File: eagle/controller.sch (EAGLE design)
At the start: 34 parts, among them K1 G5V1, T1 2SC1213, T2 2SC1213, X12 057-040-0

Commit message: First PCB
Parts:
- X1: device con-amp:USB-787616 -> con-ptr500:AK500/2
- X11: device con-ptr500:AK500/2 -> con-ptr500:AK500/3-H
- X12: value 057-040-0 -> (none); device con-panduit:057-040-0 -> con-amp:USB-787616
- X13: value (none) -> 057-040-0; device con-phoenix-254:MPT3 -> con-panduit:057-040-0
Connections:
- net GND: now also X1-2.KL, X12.4, X13-6.S, X2-1.KL; no longer X1.4, X12-6.S, X13-1.1, X2-2.KL
- net N$1: now also X1-1.KL, X2-2.KL; no longer X2-1.KL, X5-2.KL
- net N$13: now also X13-13.S, X8-2.KL; no longer X12-13.S, X3-2.KL
- net N$15: now also X13-15.S, X9-2.KL; no longer X12-15.S, X4-2.KL
- net N$17: now also X13-12.S; no longer X12-12.S
- net N$18: now also X10-2.KL, X13-22.S; no longer X12-22.S, X6-2.KL
- net N$19: now also X13-7.S; no longer X12-7.S
- net N$20: now also X13-1.S; no longer X12-1.S
- net N$21: now also X13-16.S; no longer X12-16.S
- net N$22: now also R1.2, X12.1, X6-2.KL; no longer X1.1, X11-2.KL
- net N$4: now also X11-2.KL, X3-2.KL, X4-2.KL, X5-2.KL; no longer X10-2.KL, X13-2.1, X8-2.KL, X9-2.KL
- net N$5: now also X11-3.KL, X13-39.S; no longer X12-39.S, X13-3.1
- net N$6: now also X13-11.S; no longer X12-11.S
- net N$9: now also X13-18.S; no longer X12-18.S
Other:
- moved on the sheet: X10-1, X10-2, X11-1, X11-2, X2-1, X2-2, X3-1, X3-2, X4-1, X4-2, X5-1, X5-2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

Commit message: Updating PIR
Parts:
- removed R1: 10K, resistor:R-EU_0204/7
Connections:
- net N$22: no longer R1.2
- net N$5: now also X13-37.S; no longer R1.1, X13-39.S
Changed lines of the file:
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@@
 <part name="X13" library="con-panduit" deviceset="057-040-" device="0"/>
 <part name="GND17" library="supply1" deviceset="GND" device=""/>
-<part name="R1" library="resistor" deviceset="R-EU_" device="0204/7" value="10K"/>
 <part name="LED1" library="led" deviceset="LED" device="5MM"/>
 <part name="R2" library="resistor" deviceset="R-EU_" device="0204/7" value="1.5K"/>
@@
 <instance part="X13" gate="-40" x="215.9" y="-40.64"/>
 <instance part="GND17" gate="1" x="142.24" y="-38.1"/>
-<instance part="R1" gate="G$1" x="162.56" y="-10.16" rot="R90"/>
 <instance part="LED1" gate="G$1" x="17.78" y="66.04"/>
 <instance part="R2" gate="G$1" x="17.78" y="50.8" rot="R270"/>
@@
 <wire x1="91.44" y1="71.12" x2="104.14" y2="71.12" width="0.1524" layer="91"/>
 <junction x="104.14" y="71.12"/>
-<wire x1="162.56" y1="-5.08" x2="162.56" y2="71.12" width="0.1524" layer="91"/>
-<wire x1="162.56" y1="71.12" x2="144.78" y2="71.12" width="0.1524" layer="91"/>
-<junction x="144.78" y="71.12"/>
-<pinref part="R1" gate="G$1" pin="2"/>
 </segment>
 </net>
@@
 <net name="N$5" class="0">
 <segment>
-<pinref part="R1" gate="G$1" pin="1"/>
-<wire x1="162.56" y1="-30.48" x2="162.56" y2="-15.24" width="0.1524" layer="91"/>
-<wire x1="162.56" y1="-30.48" x2="187.96" y2="-30.48" width="0.1524" layer="91"/>
-<pinref part="X13" gate="-39" pin="S"/>
-<wire x1="187.96" y1="-30.48" x2="187.96" y2="-40.64" width="0.1524" layer="91"/>
-<wire x1="187.96" y1="-40.64" x2="195.58" y2="-40.64" width="0.1524" layer="91"/>
+<wire x1="157.48" y1="-30.48" x2="190.5" y2="-30.48" width="0.1524" layer="91"/>
 <pinref part="X11" gate="-3" pin="KL"/>
 <wire x1="157.48" y1="-33.02" x2="157.48" y2="-30.48" width="0.1524" layer="91"/>
-<wire x1="157.48" y1="-30.48" x2="162.56" y2="-30.48" width="0.1524" layer="91"/>
-<junction x="162.56" y="-30.48"/>
-</segment>
-</net>
+<wire x1="190.5" y1="-30.48" x2="190.5" y2="-35.56" width="0.1524" layer="91"/>
+<pinref part="X13" gate="-37" pin="S"/>
+<wire x1="190.5" y1="-35.56" x2="195.58" y2="-35.56" width="0.1524" layer="91"/>
+</segment>
+</net>

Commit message: Update
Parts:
- removed T1, T2: 2SC1213, transistor:-NPN-TO92-EBC
- added T3, T4: 2N2222, transistor-neu-to92:2N2222-NPN-TO92-EBC
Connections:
- net GND: now also T3.E, T4.C; no longer T1.E, T2.E
- net N$10: now also T4.B; no longer T1.B
- net N$12: now also T4.E; no longer T1.C
- net N$2: now also T3.B; no longer T2.B
- net N$3: now also T3.C; no longer T2.C
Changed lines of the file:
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@@
 <part name="GND1" library="supply1" deviceset="GND" device=""/>
 <part name="R3" library="resistor" deviceset="R-EU_" device="0204/7" value="1.5K"/>
-<part name="T1" library="transistor" deviceset="*-NPN-" device="TO92-EBC" value="2SC1213"/>
 <part name="R4" library="resistor" deviceset="R-EU_" device="0204/7" value="1.3K"/>
 <part name="R5" library="resistor" deviceset="R-EU_" device="0204/7" value="10K"/>
@@
 <part name="X7" library="con-ptr500" deviceset="AK500/2" device=""/>
 <part name="GND9" library="supply1" deviceset="GND" device=""/>
-<part name="T2" library="transistor" deviceset="*-NPN-" device="TO92-EBC" value="2SC1213"/>
 <part name="R12" library="resistor" deviceset="R-EU_" device="0204/7" value="1.3K"/>
 <part name="GND8" library="supply1" deviceset="GND" device=""/>
@@
 <part name="GND18" library="supply1" deviceset="GND" device=""/>
 <part name="X11" library="con-ptr500" deviceset="AK500/3-H" device=""/>
+<part name="T3" library="transistor-neu-to92" deviceset="*-NPN-" device="TO92-EBC" technology="2N2222" value="2N2222"/>
+<part name="T4" library="transistor-neu-to92" deviceset="*-NPN-" device="TO92-EBC" technology="2N2222" value="2N2222"/>
 </parts>
 <sheets>
@@
 <instance part="GND1" gate="1" x="50.8" y="40.64"/>
 <instance part="R3" gate="G$1" x="7.62" y="15.24" rot="R90"/>
-<instance part="T1" gate="G$1" x="73.66" y="38.1" rot="MR180"/>
 <instance part="R4" gate="G$1" x="91.44" y="25.4" rot="R180"/>
 <instance part="R5" gate="G$1" x="114.3" y="7.62" rot="R90"/>
@@
 <instance part="X7" gate="-2" x="76.2" y="-40.64" rot="R90"/>
 <instance part="GND9" gate="1" x="63.5" y="-48.26"/>
-<instance part="T2" gate="G$1" x="12.7" y="-53.34"/>
 <instance part="R12" gate="G$1" x="10.16" y="-27.94" rot="R270"/>
-<instance part="GND8" gate="1" x="15.24" y="-60.96"/>
+<instance part="GND8" gate="1" x="15.24" y="-63.5"/>
 <instance part="GND10" gate="1" x="-2.54" y="-12.7"/>
 <instance part="GND11" gate="1" x="-15.24" y="58.42"/>
@@
 <instance part="X11" gate="-2" x="152.4" y="-38.1" rot="R90"/>
 <instance part="X11" gate="-3" x="157.48" y="-38.1" rot="R90"/>
+<instance part="T3" gate="G$1" x="12.7" y="-53.34"/>
+<instance part="T4" gate="G$1" x="73.66" y="38.1"/>
 </instances>
 <busses>
@@
 <junction x="50.8" y="43.18"/>
 <pinref part="GND1" gate="1" pin="GND"/>
-<junction x="76.2" y="43.18"/>
-<wire x1="76.2" y1="43.18" x2="50.8" y2="43.18" width="0.1524" layer="91"/>
-<pinref part="T1" gate="G$1" pin="E"/>
 <pinref part="OK2" gate="G$1" pin="EMIT"/>
 <wire x1="25.4" y1="43.18" x2="25.4" y2="-2.54" width="0.1524" layer="91"/>
+<wire x1="50.8" y1="43.18" x2="76.2" y2="43.18" width="0.1524" layer="91"/>
+<pinref part="X12" gate="G$1" pin="4"/>
 <wire x1="76.2" y1="43.18" x2="144.78" y2="43.18" width="0.1524" layer="91"/>
-<pinref part="X12" gate="G$1" pin="4"/>
 <wire x1="144.78" y1="43.18" x2="144.78" y2="55.88" width="0.1524" layer="91"/>
 <junction x="144.78" y="43.18"/>
 <pinref part="LED2" gate="G$1" pin="C"/>
+<pinref part="T4" gate="G$1" pin="C"/>
+<junction x="76.2" y="43.18"/>
 </segment>
 <segment>
@@
 </segment>
 <segment>
-<pinref part="T2" gate="G$1" pin="E"/>
-<pinref part="GND8" gate="1" pin="GND"/>
-</segment>
-<segment>
 <pinref part="OK2" gate="G$1" pin="C"/>
 <pinref part="GND10" gate="1" pin="GND"/>
@@
 <pinref part="GND18" gate="1" pin="GND"/>
 </segment>
+<segment>
+<pinref part="GND8" gate="1" pin="GND"/>
+<pinref part="T3" gate="G$1" pin="E"/>
+<wire x1="15.24" y1="-60.96" x2="15.24" y2="-58.42" width="0.1524" layer="91"/>
+</segment>
 </net>
 <net name="N$10" class="0">
 <segment>
-<pinref part="T1" gate="G$1" pin="B"/>
 <wire x1="71.12" y1="38.1" x2="71.12" y2="25.4" width="0.1524" layer="91"/>
 <wire x1="71.12" y1="25.4" x2="86.36" y2="25.4" width="0.1524" layer="91"/>
 <pinref part="R4" gate="G$1" pin="2"/>
+<pinref part="T4" gate="G$1" pin="B"/>
 </segment>
 </net>
 <net name="N$12" class="0">
 <segment>
-<pinref part="T1" gate="G$1" pin="C"/>
 <wire x1="76.2" y1="33.02" x2="81.28" y2="33.02" width="0.1524" layer="91"/>
 <pinref part="SG1" gate="G$1" pin="1"/>
+<pinref part="T4" gate="G$1" pin="E"/>
 </segment>
 </net>
@@
 <net name="N$2" class="0">
 <segment>
-<pinref part="T2" gate="G$1" pin="B"/>
 <wire x1="10.16" y1="-53.34" x2="10.16" y2="-33.02" width="0.1524" layer="91"/>
 <pinref part="R12" gate="G$1" pin="2"/>
+<pinref part="T3" gate="G$1" pin="B"/>
 </segment>
 </net>
@@
 <wire x1="20.32" y1="-48.26" x2="15.24" y2="-48.26" width="0.1524" layer="91"/>
 <junction x="20.32" y="-48.26"/>
-<pinref part="T2" gate="G$1" pin="C"/>
-</segment>
-</net>
+<pinref part="T3" gate="G$1" pin="C"/>
+</segment>
+</net>

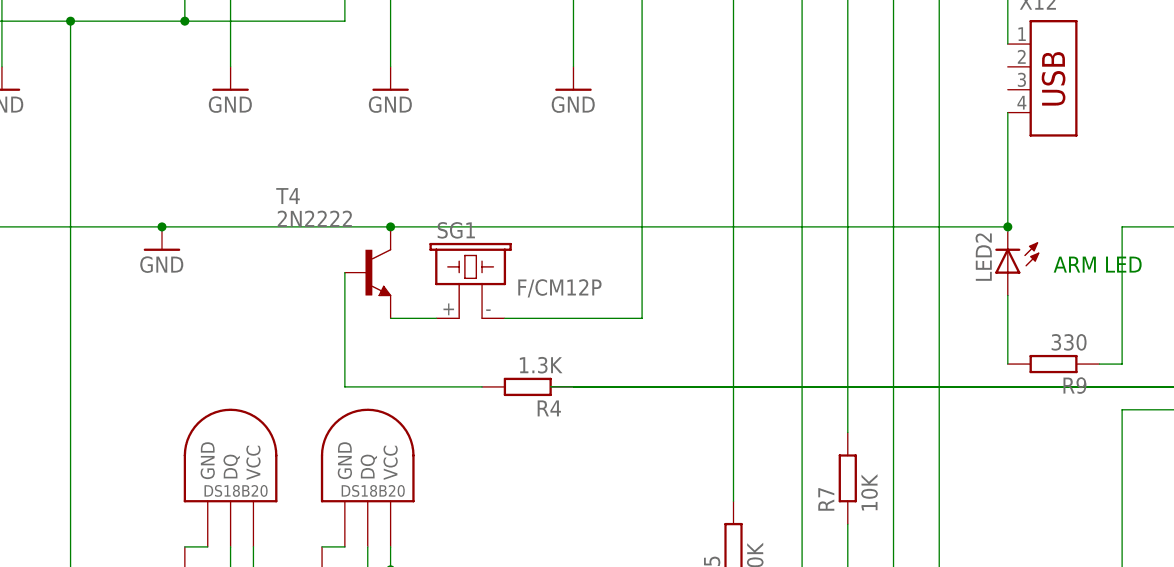
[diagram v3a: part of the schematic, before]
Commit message: Fixing schematic bug
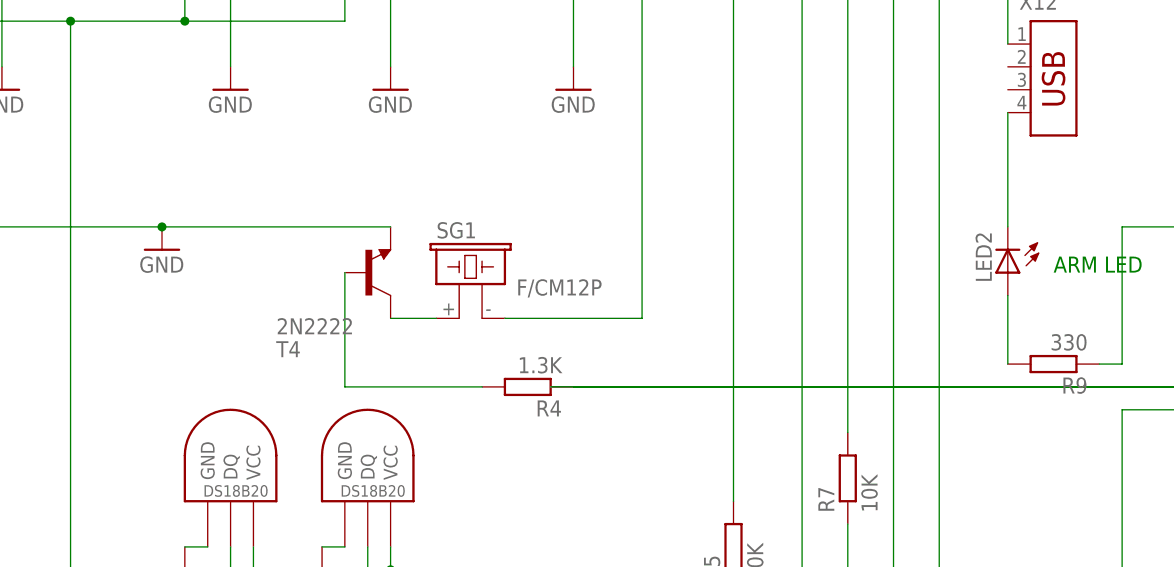
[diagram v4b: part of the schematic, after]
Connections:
- new net N$11: LED2.C, X12.4
- net GND: now also T4.E; no longer LED2.C, T4.C, X12.4
- net N$12: now also T4.C; no longer T4.E
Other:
- moved on the sheet: T4
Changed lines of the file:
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@@
 <instance part="X11" gate="-3" x="157.48" y="-38.1" rot="R90"/>
 <instance part="T3" gate="G$1" x="12.7" y="-53.34"/>
-<instance part="T4" gate="G$1" x="73.66" y="38.1"/>
+<instance part="T4" gate="G$1" x="73.66" y="38.1" rot="MR180"/>
 </instances>
 <busses>
@@
 <net name="GND" class="3">
 <segment>
+<pinref part="OK2" gate="G$1" pin="EMIT"/>
+<pinref part="GND1" gate="1" pin="GND"/>
 <wire x1="25.4" y1="43.18" x2="50.8" y2="43.18" width="0.1524" layer="91"/>
+<wire x1="25.4" y1="43.18" x2="25.4" y2="-2.54" width="0.1524" layer="91"/>
+<pinref part="T4" gate="G$1" pin="E"/>
+<wire x1="76.2" y1="43.18" x2="50.8" y2="43.18" width="0.1524" layer="91"/>
 <junction x="50.8" y="43.18"/>
-<pinref part="GND1" gate="1" pin="GND"/>
-<pinref part="OK2" gate="G$1" pin="EMIT"/>
-<wire x1="25.4" y1="43.18" x2="25.4" y2="-2.54" width="0.1524" layer="91"/>
-<wire x1="50.8" y1="43.18" x2="76.2" y2="43.18" width="0.1524" layer="91"/>
-<pinref part="X12" gate="G$1" pin="4"/>
-<wire x1="76.2" y1="43.18" x2="144.78" y2="43.18" width="0.1524" layer="91"/>
-<wire x1="144.78" y1="43.18" x2="144.78" y2="55.88" width="0.1524" layer="91"/>
-<junction x="144.78" y="43.18"/>
-<pinref part="LED2" gate="G$1" pin="C"/>
-<pinref part="T4" gate="G$1" pin="C"/>
-<junction x="76.2" y="43.18"/>
 </segment>
 <segment>
@@
 <net name="N$10" class="0">
 <segment>
-<wire x1="71.12" y1="38.1" x2="71.12" y2="25.4" width="0.1524" layer="91"/>
 <wire x1="71.12" y1="25.4" x2="86.36" y2="25.4" width="0.1524" layer="91"/>
 <pinref part="R4" gate="G$1" pin="2"/>
 <pinref part="T4" gate="G$1" pin="B"/>
-</segment>
-</net>
-<net name="N$12" class="0">
-<segment>
-<wire x1="76.2" y1="33.02" x2="81.28" y2="33.02" width="0.1524" layer="91"/>
-<pinref part="SG1" gate="G$1" pin="1"/>
-<pinref part="T4" gate="G$1" pin="E"/>
+<wire x1="71.12" y1="25.4" x2="71.12" y2="38.1" width="0.1524" layer="91"/>
 </segment>
 </net>
@@
 </segment>
 </net>
+<net name="N$11" class="3">
+<segment>
+<pinref part="X12" gate="G$1" pin="4"/>
+<wire x1="144.78" y1="43.18" x2="144.78" y2="55.88" width="0.1524" layer="91"/>
+<pinref part="LED2" gate="G$1" pin="C"/>
+</segment>
+</net>
+<net name="N$12" class="0">
+<segment>
+<pinref part="T4" gate="G$1" pin="C"/>
+<pinref part="SG1" gate="G$1" pin="1"/>
+<wire x1="76.2" y1="33.02" x2="81.28" y2="33.02" width="0.1524" layer="91"/>
+</segment>
+</net>

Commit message: Small redesign. Bugfixes
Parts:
- removed X2, X3: (no value), con-ptr500:AK500/2
- added D1: 1N5822, diode:SCHOTTKY-DIODEDO201T15
- R2, R3: value 1.5K -> 880
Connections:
- removed net N$12: SG1.1, T4.C
- net GND: now also LED2.C, X1-1.KL, X12.4; no longer X1-2.KL, X2-1.KL, X3-1.KL
- net N$1: now also D1.A, X1-2.KL; no longer X1-1.KL, X2-2.KL
- net N$11: now also SG1.2, T4.C; no longer LED2.C, X12.4
- net N$22: now also SG1.1; no longer SG1.2
- net N$4: now also D1.C; no longer X3-2.KL
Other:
- note added: "13.7V"
- note removed: "24V"
- note removed: "From 24-13.5V DC-DC"
- note removed: "To 24-13.5V DC-DC"
- moved on the sheet: LED1, LED2, R10, R5, R9, SG1, T4, X1-1, X1-2, X12

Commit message: Board update
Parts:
- removed X10: (no value), con-ptr500:AK500/2
- removed X11: (no value), con-ptr500:AK500/3-H
- added X2, X3: (no value), con-ptr500:AK500/2
- X9: device con-ptr500:AK500/2 -> con-ptr500:AK500/3-H
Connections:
- net GND: now also X2-1.KL, X3-1.KL; no longer X10-1.KL, X11-1.KL
- net N$13: now also X6-2.KL; no longer X8-2.KL
- net N$15: now also X7-2.KL; no longer X9-2.KL
- net N$18: now also X8-2.KL; no longer X10-2.KL
- net N$22: now also X4-2.KL; no longer X6-2.KL
- net N$23: now also X5-2.KL; no longer X7-2.KL
- net N$4: now also X2-2.KL, X3-2.KL, X9-2.KL; no longer X11-2.KL, X4-2.KL, X5-2.KL
- net N$5: now also X9-3.KL; no longer X11-3.KL
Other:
- moved on the sheet: X4-1, X4-2, X5-1, X5-2, X6-1, X6-2, X7-1, X7-2, X8-1, X8-2, X9-1, X9-2
